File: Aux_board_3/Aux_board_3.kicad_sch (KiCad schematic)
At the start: 0 parts

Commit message: Board 3 schematic almost done
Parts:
- added C1, C2, C3, C4: 47u, Capacitor_SMD:C_0805_2012Metric_Pad1.18x1.45mm_HandSolder, symbol Device:C
- added D1, D2, D3: LED_G, LED_SMD:LED_0805_2012Metric_Pad1.15x1.40mm_HandSolder, symbol Device:LED
- added J1: P11d, Connector_Dsub:DSUB-25_Male_Horizontal_P2.77x2.84mm_EdgePinOffset7.70mm_Housed_MountingHolesOffset9.12mm, symbol Connector:DB25_Plug_MountingHoles
- added J12: ~, Connector_PinHeader_2.54mm:PinHeader_2x04_P2.54mm_Horizontal, symbol Connector_Generic:Conn_02x04_Odd_Even
- added J4: R_LIM_MAX, Connector_PinHeader_2.54mm:PinHeader_1x03_P2.54mm_Horizontal, symbol Connector:Conn_01x03_Pin
- added J5: R_HOME, Connector_PinHeader_2.54mm:PinHeader_1x03_P2.54mm_Horizontal, symbol Connector:Conn_01x03_Pin
- added Q1, Q3, Q5: BSS138KJ, Package_TO_SOT_SMD:SOT-23, symbol Transistor_FET:BSS138
- added Q2, Q4, Q6: BSS84KJ, Package_TO_SOT_SMD:SOT-23, symbol Transistor_FET:BSS84
- added R1: 2k2, Resistor_SMD:R_0805_2012Metric_Pad1.20x1.40mm_HandSolder, symbol Device:R
- added R10, R15, R16, R21, R22, R9: 560R, Resistor_SMD:R_0805_2012Metric_Pad1.20x1.40mm_HandSolder, symbol Device:R
- added R11, R12, R13, R17, R18, R19, R5, R6, R7: 0R, Resistor_SMD:R_0805_2012Metric_Pad1.20x1.40mm_HandSolder, symbol Device:R
- added R14, R20, R8: 4k7, Resistor_SMD:R_0805_2012Metric_Pad1.20x1.40mm_HandSolder, symbol Device:R
- added R2: 330R, Resistor_SMD:R_0805_2012Metric_Pad1.20x1.40mm_HandSolder, symbol Device:R
- added R3: 150R, Resistor_SMD:R_0805_2012Metric_Pad1.20x1.40mm_HandSolder, symbol Device:R
- added TP1: GND, TestPoint:TestPoint_Pad_2.0x2.0mm, symbol Connector:TestPoint_Alt
- added TP2: 24V, TestPoint:TestPoint_Pad_2.0x2.0mm, symbol Connector:TestPoint_Alt
- added TP3: 5V, TestPoint:TestPoint_Pad_2.0x2.0mm, symbol Connector:TestPoint_Alt
- added TP4: 3V3, TestPoint:TestPoint_Pad_2.0x2.0mm, symbol Connector:TestPoint_Alt
- added U1: DSN-1504-3A, power_modules:DSN-1504-3A, symbol power_modules:DSN-1504-3A
- added U2: AMS1117-3.3, Package_TO_SOT_SMD:SOT-223-3_TabPin2, symbol Regulator_Linear:AMS1117-3.3
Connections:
- new net +24V: C1.1, J1.13, J1.25 (P25), Q2.3 (D), Q4.3 (D), Q6.3 (D), R1.1, R11.1, R15.1, R17.1, R21.1, R5.1, R9.1, TP2.1, U1.1 (Vin+), U1.2 (Vin+)
- new net +3V3: C4.1, R13.1, R19.1, R3.1, R7.1, TP4.1, U2.2 (VO)
- new net +5V: C2.1, C3.1, R12.1, R18.1, R2.1, R6.1, TP3.1, U1.7 (Vout+), U1.8 (Vout+), U2.3 (VI)
- new net ALF_ENC_A: J1.3
- new net ALF_ENC_B: J1.16 (P16)
- new net ALF_LIM_1: J1.6
- new net ALF_LIM_2: J1.19 (P19)
- new net BET_ENC_A: J1.4
- new net BET_ENC_B: J1.17 (P17)
- new net BET_LIM_1: J1.7
- new net BET_LIM_2: J1.20 (P20)
- new net GND: C1.2, C2.2, C3.2, C4.2, D1.1 (K), D2.1 (K), D3.1 (K), J1.11, J1.15 (P15), J1.18 (P18), J1.2, J1.21 (P21), J1.5, J1.8, J4.1 (Pin_1), J5.1 (Pin_1), Q1.2 (S), Q3.2 (S), Q5.2 (S), R10.2, R16.2, R22.2, TP1.1, U1.3 (Vin-), U1.4 (Vin-), U1.5 (Vout-), U1.6 (Vout-), U2.1 (GND)
- new net LED24_A: D1.2 (A), R1.2
- new net LED33_A: D3.2 (A), R3.2
- new net LED5_A: D2.2 (A), R2.2
- new net R_HOME: J1.12, Q6.2 (S), R22.1
- new net R_HOME_IN: J5.2 (Pin_2), R20.2
- new net R_HOME_NG: Q5.3 (D), Q6.1 (G), R21.2
- new net R_HOME_PG: Q5.1 (G), R20.1
- new net R_HOME_PWR: J5.3 (Pin_3), R17.2, R18.2, R19.2
- new net R_LIM_MAX: J1.23 (P23), Q4.2 (S), R16.1
- new net R_LIM_MAX_IN: J4.2 (Pin_2), R14.2
- new net R_LIM_MAX_NG: Q3.1 (G), R14.1
- new net R_LIM_MAX_PG: Q3.3 (D), Q4.1 (G), R15.2
- new net R_LIM_MAX_PWR: J4.3 (Pin_3), R11.2, R12.2, R13.2
- new net R_LIM_MIN: J1.10, Q2.2 (S), R10.1
- new net R_LIM_MIN_IN: R8.2
- new net R_LIM_MIN_NG: Q1.1 (G), R8.1
- new net R_LIM_MIN_PG: Q1.3 (D), Q2.1 (G), R9.2
- new net R_LIM_MIN_PWR: R5.2, R6.2, R7.2
- new net TH_ENC_A: J1.1
- new net TH_ENC_B: J1.14 (P14)
- new net TH_HOME: J1.24 (P24)
- new net TH_LIM_MAX: J1.9
- new net TH_LIM_MIN: J1.22 (P22)
- no-connect marks 0 -> 1
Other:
- added sheet ALPHA AXIS (Aux_board_3_alf.kicad_sch)
- added sheet BETA AXIS (Aux_board_3_bet.kicad_sch)
- added sheet END-EFFECTOR (Aux_board_3_ee.kicad_sch)
- added sheet RIGHT_ANGLE HEADERS (Aux_board_3_headers.kicad_sch)
- added sheet THETA AXIS (Aux_board_3_th.kicad_sch)
- note added: "CONN & POWER INSIDE DUAL POWER!"
- note added: "Connection to Aux. Board 1"
- note added: "Power (24V to 5V stepdown, 5V to 3V3 LDO)"
- note added: "R axis limit & homing sensors level shifting to 24V"

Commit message: finished Board 3 schematic
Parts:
- removed J12: ~, Connector_PinHeader_2.54mm:PinHeader_2x04_P2.54mm_Horizontal, symbol Connector_Generic:Conn_02x04_Odd_Even
- removed J4: R_LIM_MAX, Connector_PinHeader_2.54mm:PinHeader_1x03_P2.54mm_Horizontal, symbol Connector:Conn_01x03_Pin
- removed J5: R_HOME, Connector_PinHeader_2.54mm:PinHeader_1x03_P2.54mm_Horizontal, symbol Connector:Conn_01x03_Pin
- removed Q1, Q3, Q5: BSS138KJ, Package_TO_SOT_SMD:SOT-23, symbol Transistor_FET:BSS138
- removed Q2, Q4, Q6: BSS84KJ, Package_TO_SOT_SMD:SOT-23, symbol Transistor_FET:BSS84
- removed R10, R22, R9: 560R, Resistor_SMD:R_0805_2012Metric_Pad1.20x1.40mm_HandSolder, symbol Device:R
- removed R11, R12, R5, R6, R7: 0R, Resistor_SMD:R_0805_2012Metric_Pad1.20x1.40mm_HandSolder, symbol Device:R
- removed R8: 4k7, Resistor_SMD:R_0805_2012Metric_Pad1.20x1.40mm_HandSolder, symbol Device:R
- added J10: R_HOME, Connector_PinHeader_2.54mm:PinHeader_1x03_P2.54mm_Horizontal, symbol Connector:Conn_01x03_Pin
- added J11: R_LIM_MAX, Connector_PinHeader_2.54mm:PinHeader_1x03_P2.54mm_Horizontal, symbol Connector:Conn_01x03_Pin
- added J4, J5, J6, J7, J8, J9: ~, Connector_PinHeader_2.54mm:PinHeader_2x04_P2.54mm_Horizontal, symbol Connector_Generic:Conn_02x04_Odd_Even
- R14, R20: value 4k7 -> 0R; Sourced 1 -> 0; Supplier Lomex -> LCSC; Supplier URL (none) -> https://www.lcsc.com/product-detail/Chip-Resistor-Surface-M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; Supplier item no 81-10-95 -> C304192
- R15, R16, R21: value 560R -> 0R; Sourced 1 -> 0; Supplier Lomex -> LCSC; Supplier URL (none) -> https://www.lcsc.com/product-detail/Chip-Resistor-Surface-M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; Supplier item no 81-10-84 -> C304192; now not fitted
- R17: now fitted
- R18: now not fitted
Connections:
- net R_HOME_PG is gone; now on net +5V: R20.1
- net R_LIM_MAX_NG is gone; now on net +5V: R14.1
- net R_LIM_MAX_PWR is gone; now on net ENC_PWR: R13.2
- net +24V: now also R13.1, R16.1, R19.1; no longer R15.1, R17.1, R21.1
- net +3V3: now also R15.1, R18.1, R21.1; no longer R13.1, R19.1
- net +5V: now also R17.1, J6.3 (Pin_3), J6.4 (Pin_4), J9.4 (Pin_4); no longer R18.1
- net GND: now also J10.3 (Pin_3), J11.3 (Pin_3), J4.5 (Pin_5), J5.3 (Pin_3), J5.4 (Pin_4), J6.1 (Pin_1), J6.2 (Pin_2), J6.7 (Pin_7), J6.8 (Pin_8), J7.6 (Pin_6), J7.7 (Pin_7), J8.4 (Pin_4), J8.7 (Pin_7), J9.2 (Pin_2), J9.7 (Pin_7), J9.8 (Pin_8); no longer R16.2
- net R_HOME_IN: now also J10.2 (Pin_2); no longer R20.2
- net R_LIM_MAX: no longer R16.1
- net R_LIM_MAX_IN: now also J11.2 (Pin_2); no longer R14.2
- net R_LIM_MIN_IN: now also J5.2 (Pin_2)
- net TH_HOME: now also J5.8 (Pin_8)
- net R_HOME_NG renamed HOME_PWR
- net HOME_PWR: now also R19.2, R20.2, J10.1 (Pin_1), J5.6 (Pin_6)
- net R_HOME_PWR renamed LIM_PWR
- net LIM_PWR: now also R16.2, J11.1 (Pin_1), J4.1 (Pin_1), J4.7 (Pin_7), J4.8 (Pin_8), J5.5 (Pin_5), J7.2 (Pin_2), J7.8 (Pin_8), J8.6 (Pin_6); no longer R19.2
- net R_LIM_MAX_PG renamed ENC_PWR
- net ENC_PWR: now also R14.2, J7.1 (Pin_1), J8.1 (Pin_1), J9.1 (Pin_1)
- new net ALF_ENC_A_IN: J8.3 (Pin_3)
- new net ALF_ENC_B_IN: J8.5 (Pin_5)
- new net ALF_LIM_MAX_IN: J5.1 (Pin_1)
- new net ALF_LIM_MIN_IN: J8.2 (Pin_2)
- new net BET_ENC_A_IN: J7.3 (Pin_3)
- new net BET_ENC_B_IN: J7.5 (Pin_5)
- new net BET_LIM_MAX_IN: J4.3 (Pin_3)
- new net BET_LIM_MIN_IN: J7.4 (Pin_4)
- new net SRV1_PWM: J9.6 (Pin_6)
- new net SRV2_PWM: J6.5 (Pin_5)
- new net SRV3_PWM: J6.6 (Pin_6)
- new net TH_ENC_A_IN: J9.3 (Pin_3)
- new net TH_ENC_B_IN: J9.5 (Pin_5)
- new net TH_LIM_MAX_IN: J5.7 (Pin_7)
- new net TH_LIM_MIN_IN: J8.8 (Pin_8)
- no-connect marks 1 -> 4
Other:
- removed sheet ALPHA AXIS
- removed sheet BETA AXIS
- removed sheet RIGHT_ANGLE HEADERS
- removed sheet THETA AXIS
- added sheet ALPHA & BETA AXIS LEVEL SHIFTING (Aux_board_3_ALF_BET.kicad_sch)
- added sheet R & THETA AXIS LEVEL SHIFTING (Aux_board_3_R_TH.kicad_sch)
- note added: "Power selectors"
- note added: "Sensor input, servo output headers"
- note removed: "R axis limit & homing sensors level shifting to 24V"

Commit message: Board 3 layout started
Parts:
- J10, J11: Supplier (none) -> LEGOlab; Supplier item no (none) -> -
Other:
- sheet ALPHA & BETA AXIS LEVEL SHIFTING ports: added none; removed ALF_SENSORS_IN, ALF_SENSORS_OUT, BET_SENSORS_IN, BET_SENSORS_OUT
- sheet END-EFFECTOR ports: added SRV1_PWM, SRV2_PWM, SRV3_PWM; removed SERVOS
- sheet R & THETA AXIS LEVEL SHIFTING ports: added none; removed R_SENSORS_IN, R_SENSORS_OUT, TH_SENSORS_IN, TH_SENSORS_OUT

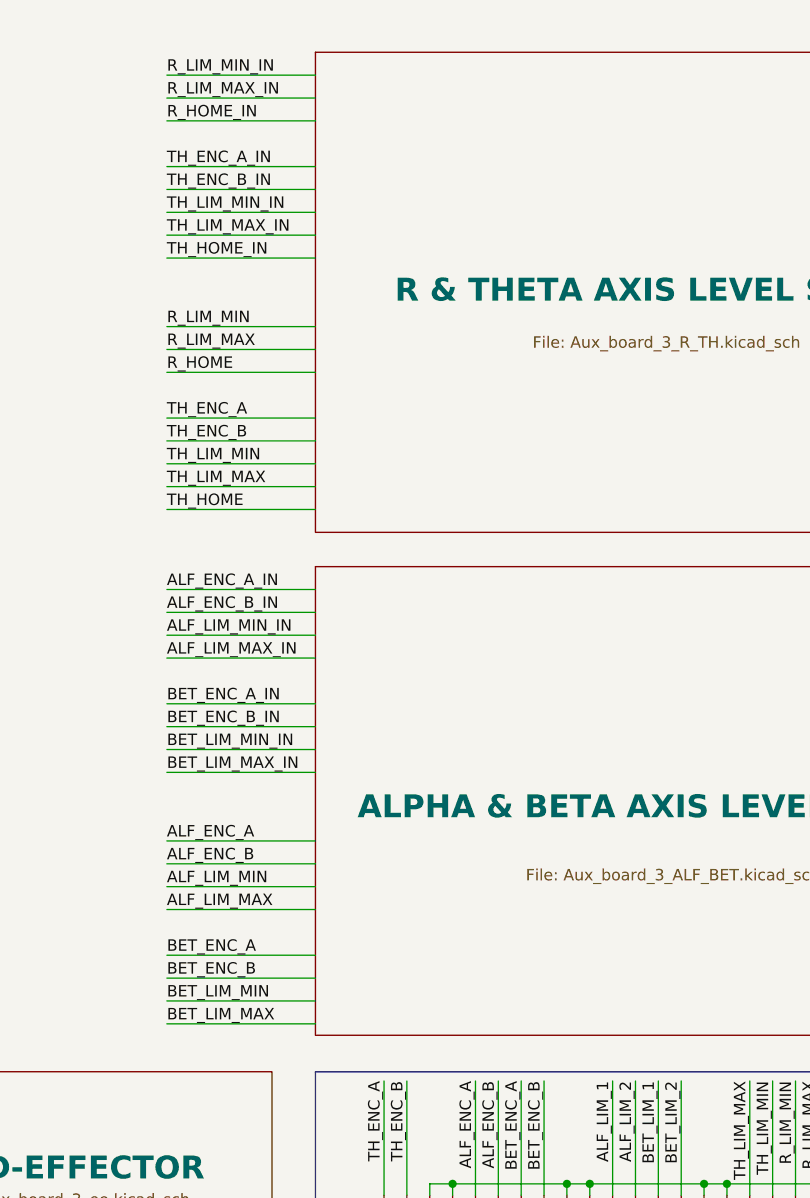
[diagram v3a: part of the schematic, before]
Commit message: Board 3 MODBUS and servos done
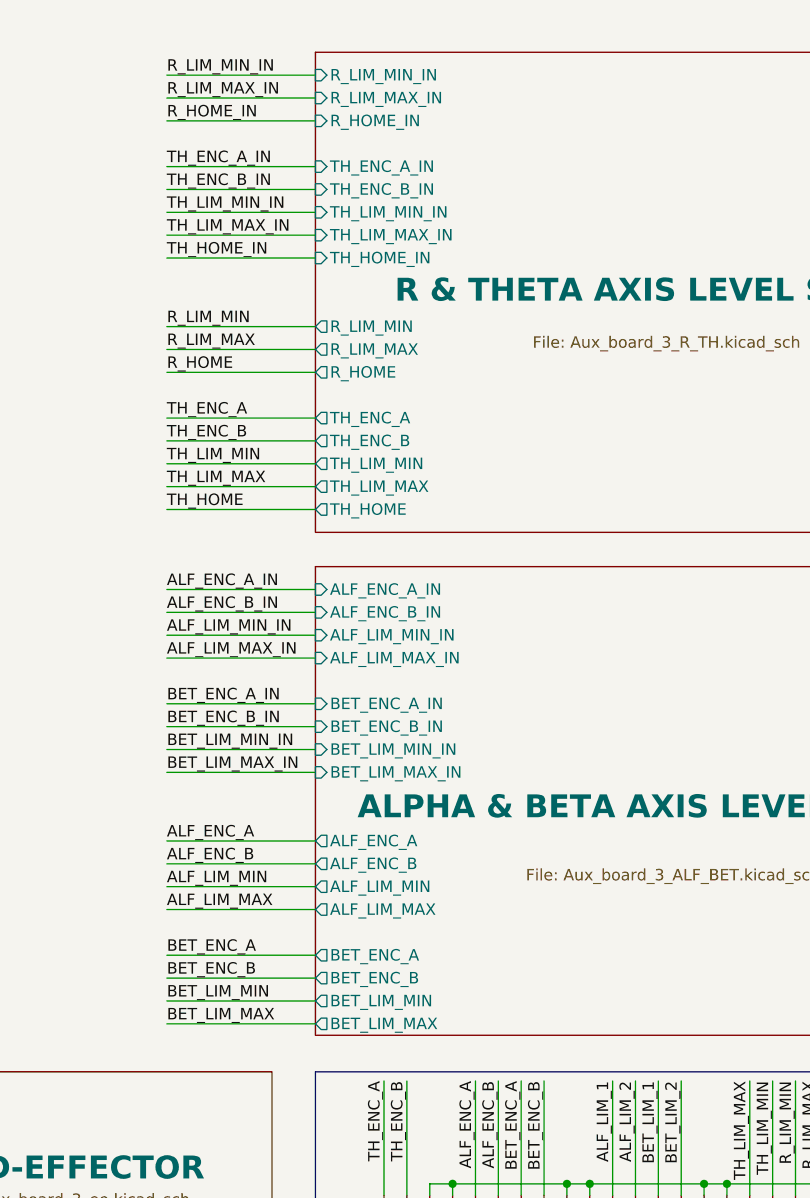
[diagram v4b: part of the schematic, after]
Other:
- sheet ALPHA & BETA AXIS LEVEL SHIFTING ports: added ALF_ENC_A, ALF_ENC_A_IN, ALF_ENC_B, ALF_ENC_B_IN, ALF_LIM_MAX, ALF_LIM_MAX_IN, ALF_LIM_MIN, ALF_LIM_MIN_IN, BET_ENC_A, BET_ENC_A_IN, BET_ENC_B, BET_ENC_B_IN, BET_LIM_MAX, BET_LIM_MAX_IN, BET_LIM_MIN, BET_LIM_MIN_IN; removed none
- sheet R & THETA AXIS LEVEL SHIFTING ports: added R_HOME, R_HOME_IN, R_LIM_MAX, R_LIM_MAX_IN, R_LIM_MIN, R_LIM_MIN_IN, TH_ENC_A, TH_ENC_A_IN, TH_ENC_B, TH_ENC_B_IN, TH_HOME, TH_HOME_IN, TH_LIM_MAX, TH_LIM_MAX_IN, TH_LIM_MIN, TH_LIM_MIN_IN; removed none
